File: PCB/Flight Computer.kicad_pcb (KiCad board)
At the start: 6 copper layers, 30 x 60 mm, 75 parts, among them J501 Conn_02x03_Counter_Clockwise, J502 USB_C_Receptacle_USB2.0_16P, J503 Screw_Terminal_01x06, J504 Screw_Terminal_01x04, J505 Conn_01x04, J506 Conn_02x03_Counter_Clockwise, J507 Conn_01x05, J601 Conn_Coaxial, Q701 SL2302S, Q702 SL2302S, Q703 SL2302S, U201 LM1117MP-3.3, U301 W25Q128JVS, U302 STM32F446RETx, U401 MMC5633NJL, U402 LSM6DSV320, U403 MS5607-02BA, U404 SAM-M8Q, U601 RFM95W-915S2, Y301 Resonator

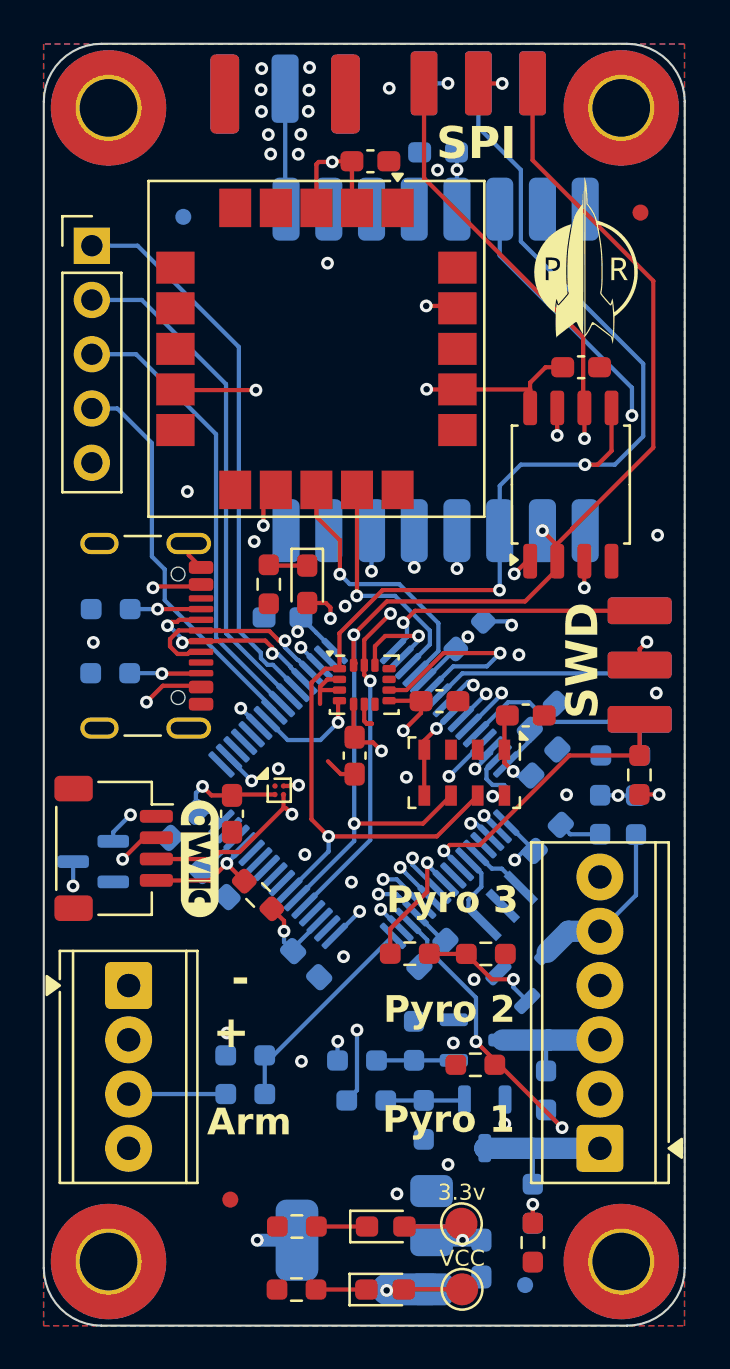
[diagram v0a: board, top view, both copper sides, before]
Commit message: Added buzzer Added 2 more leds to MCU Fixed servo connector GND hole shape Added Servo VCC pin Added additional silkscreen for debug connections Added copper plane text "V1.1" Made 915MHz radio trace 50 Ohm
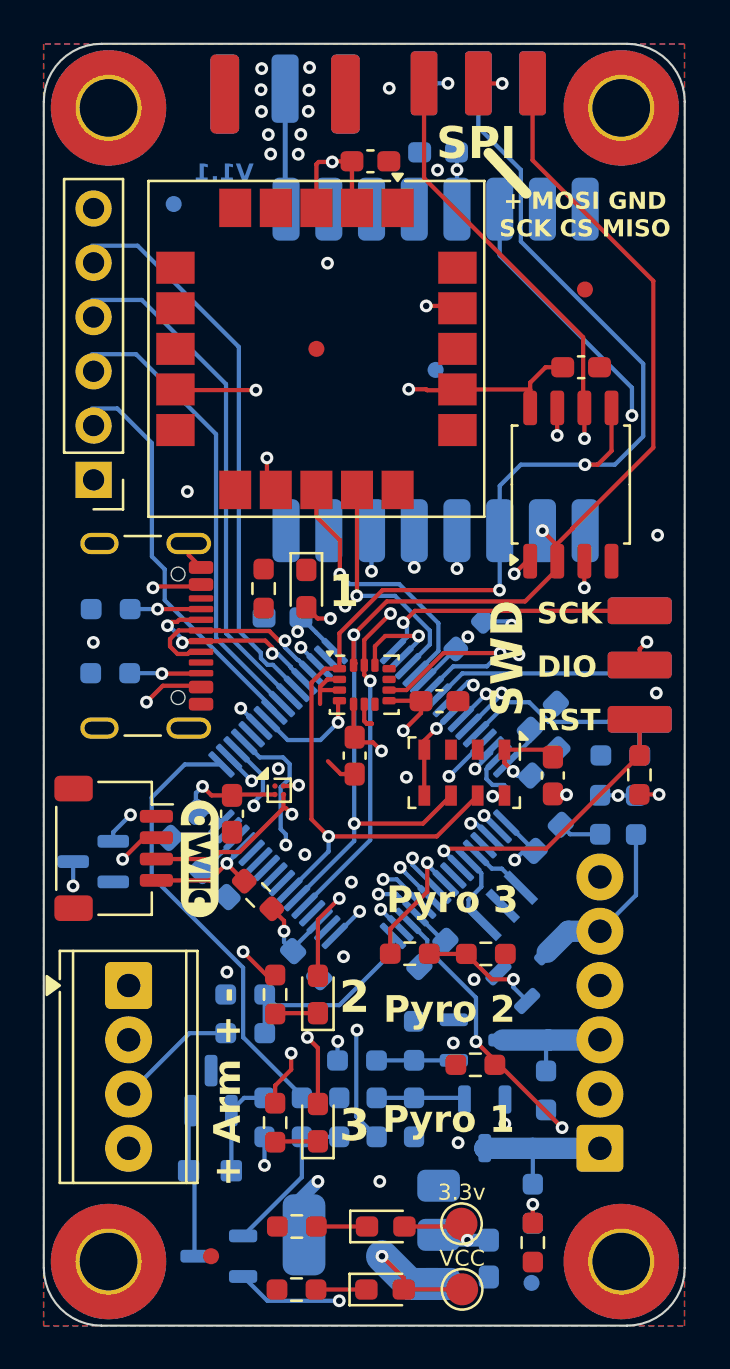
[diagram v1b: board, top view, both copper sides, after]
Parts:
- added BZ501: Buzzer, Buzzer:Buzzer_3mm, B.Cu at (105.4, 105.2)
- added D301: LED, LED_SMD:LED_0603_1608Metric_Pad1.05x0.95mm_HandSolder, F.Cu at (110.0, 78.0)
- added D303: LED, LED_SMD:LED_0603_1608Metric_Pad1.05x0.95mm_HandSolder, F.Cu at (110.5, 103.0)
- added D502: D, Package_TO_SOT_SMD:SOT-23, B.Cu at (105.5, 101.5)
- added FID102: Fiducial, Fiducial:Fiducial_0.75mm_Mask1.5mm, F.Cu at (110.4, 66.8)
- added FID202: Fiducial, Fiducial:Fiducial_0.75mm_Mask1.5mm, B.Cu at (116.0, 67.8)
- added Q1: SL2302S, Package_TO_SOT_SMD:SOT-23-3, B.Cu at (105.9, 109.2)
- added R1: 500, Resistor_SMD:R_0603_1608Metric_Pad0.98x0.95mm_HandSolder, B.Cu at (109.8, 102.8)
- added R2: 10k, Resistor_SMD:R_0603_1608Metric_Pad0.98x0.95mm_HandSolder, B.Cu at (111.5, 102.8)
- added R305: 1k, Resistor_SMD:R_0603_1608Metric_Pad0.98x0.95mm_HandSolder, F.Cu at (108.0, 78.0)
- added R307: 1k, Resistor_SMD:R_0603_1608Metric_Pad0.98x0.95mm_HandSolder, F.Cu at (108.5, 103.0)
- added R503: R_US, Resistor_SMD:R_0603_1608Metric_Pad0.98x0.95mm_HandSolder, B.Cu at (108.0, 102.8)
- G***, J503: moved to B.Cu
- J507: value Conn_01x05 -> Conn_01x06; footprint Connector_PinHeader_2.54mm:PinHeader_1x05_P2.54mm_Vertical -> Connector_PinHeader_2.54mm:PinHeader_1x06_P2.54mm_Vertical
- moved D302 19.2 mm to (110.5, 97.0), turned to 90 degrees
- moved R306 19.2 mm to (108.5, 97.0), turned to -90 degrees
- moved G*** 17.7 mm to (105.2, 63.5), turned to 180 degrees
- moved J507 11.0 mm to (100.0, 72.9), turned to 180 degrees
- moved FID101 4.44 mm to (123.0, 64.0)
- moved C404 3.08 mm to (121.5, 86.8), turned to -90 degrees
- moved R701 2.85 mm to (107.1, 98.8)
- moved R704 2.85 mm to (107.1, 97.0)
- moved FID103 2.80 mm to (105.5, 109.2)
- moved R702 0.93 mm to (113.2, 102.8), turned to 90 degrees
- moved FID201 0.75 mm to (103.8, 60.0)
- moved R705 0.47 mm to (115.0, 102.8)
- moved U201 0.41 mm to (113.0, 108.2)
- moved C201 0.35 mm to (118.5, 109.4)
- moved FID203 0.32 mm to (120.5, 110.5)
- renumbered D301 to D302, FID102 to FID103, FID103 to FID201, FID104 to FID203, R305 to R306
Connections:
- D302 pad 2: /MCU_LED -> /MCU_LED2
- J507 pad 1: /Servo1 -> GND
- J507 pad 2: /Servo2 -> VCC
- J507 pad 3: /Servo3 -> /Servo4
- J507 pad 4: /Servo4 -> /Servo3
- J507 pad 5: GND -> /Servo2
- U302 pad 34: /MCU_LED -> /MCU_LED1
- U302 pad 35: /MCU/PB14 -> /MCU_LED2
- U302 pad 36: /MCU/PB15 -> /MCU_LED3
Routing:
- net VCC: track 43.1 -> 81.9 mm, vias 2 -> 3
- net /Buzzer: track 0.00 -> 20.9 mm
- net /MCU_LED3: track 0.00 -> 19.4 mm, vias 0 -> 2
- net /MCU_LED2: track 0.00 -> 14.2 mm, vias 0 -> 2
- net /MCU_LED: track 13.5 -> 0.00 mm, vias 2 -> 0
- net /MCU_LED1: track 0.00 -> 13.1 mm, vias 0 -> 2
- net GND: track 14.6 -> 24.2 mm, vias 34 -> 35
- net Net-(Q1-G): track 0.00 -> 7.53 mm
- net Net-(BZ501--): track 0.00 -> 7.09 mm
- net Net-(BZ501-+): track 0.00 -> 4.61 mm
- net /I2C_SCL: track 27.3 -> 31.1 mm
- net Net-(D303-K): track 0.00 -> 2.07 mm
- net +3.3V: track 64.5 -> 66.5 mm
- net /Pyro1_Trigger: track 14.0 -> 15.5 mm
- net Pyro_Power: track 44.6 -> 45.8 mm
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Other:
- board text added: "+"
- board text added: "+ Arm + -"
- board text added: "+ MOSI GND SCK CS MISO"
- board text added: "-"
- board text added: "1"
- board text added: "2"
- board text added: "3"
- board text added: "4"
- board text added: "B"
- board text added: "DIO"
- board text added: "GND"
- board text added: "RST"
- board text added: "SCK"
- board text added: "SWO"
- board text added: "Servos"
- board text added: "V1.1"
- board text removed: "+ -"
- board text removed: "Arm"

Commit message: Fixed some mistakes
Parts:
- J503: moved to F.Cu
- moved R701 0.33 mm to (107.0, 98.5)
- moved R704 0.27 mm to (107.0, 96.8)
- moved D502 0.19 mm to (105.5, 101.3)
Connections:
- R503 pad 1: VCC -> +3.3V
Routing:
- net +3.3V: track 66.5 -> 68.2 mm, vias 17 -> 18
- net VCC: track 81.9 -> 80.6 mm, vias 3 -> 2
- net /Servo4: track 18.4 -> 19.4 mm
- net /Servo3: track 21.3 -> 21.9 mm
- net /Servo1: track 26.1 -> 26.8 mm
- net /Servo2: track 23.8 -> 24.4 mm

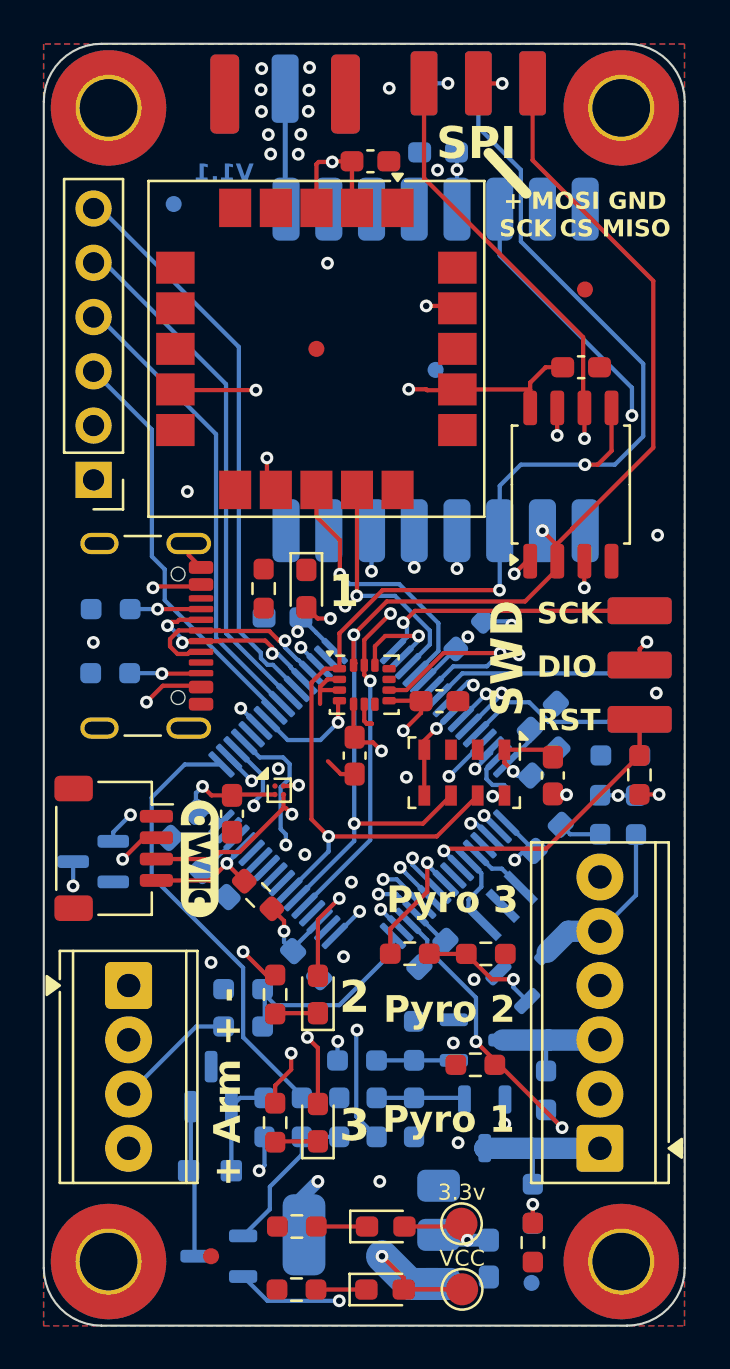
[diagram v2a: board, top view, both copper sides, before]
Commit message: Switched MISO and MOSI for IMU, fixed some DRC Errors
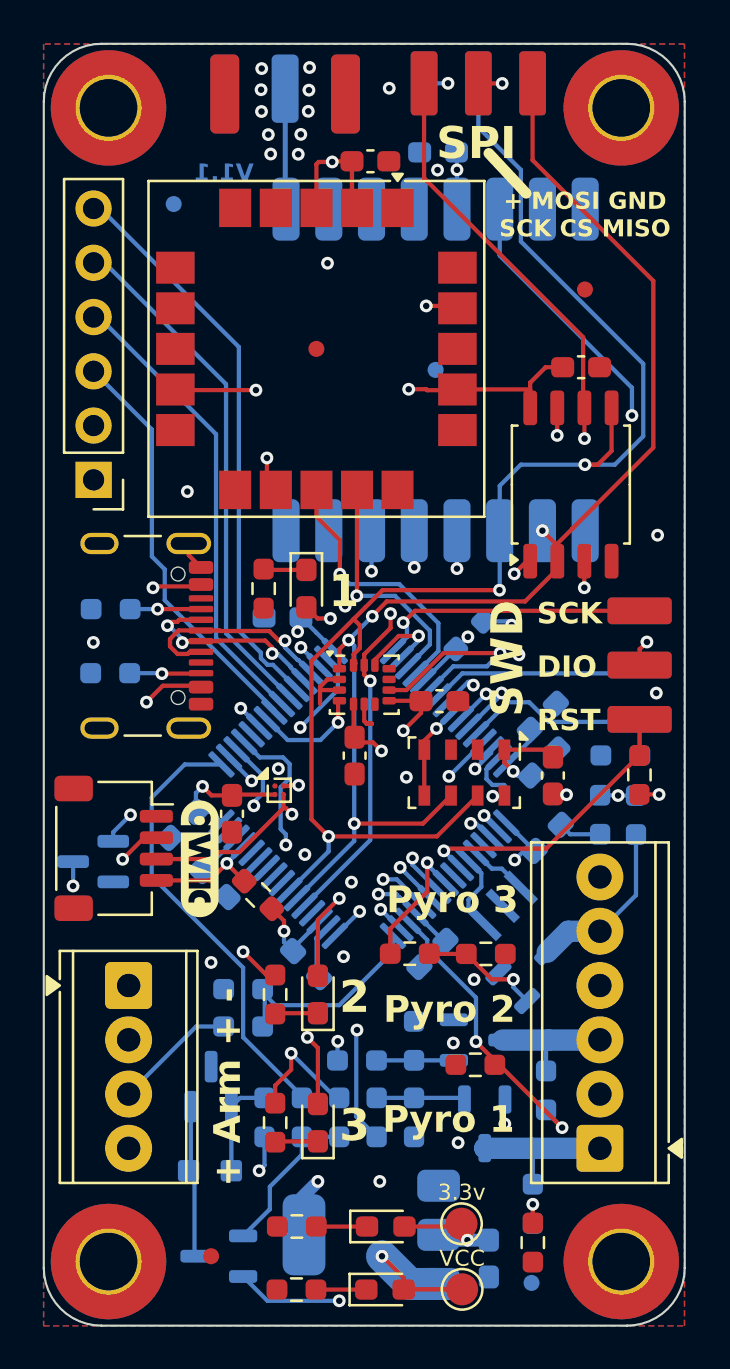
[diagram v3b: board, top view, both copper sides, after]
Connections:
- U402 pad 1: /SPI_MOSI -> /SPI_MISO
- U402 pad 14: /SPI_MISO -> /SPI_MOSI
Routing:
- net GND: track 24.2 -> 31.8 mm, vias 35 -> 36
- net /SPI_MOSI: track 66.1 -> 68.4 mm
- net Net-(D301-K): track 0.05 -> 2.07 mm
- net VCC: track 80.6 -> 79.3 mm
- net /SPI_MISO: vias 3 -> 4
- added copper zone on In1.Cu, net VCC

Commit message: Tweaked silkscreen, update via count for 3.3V reg VCC trace
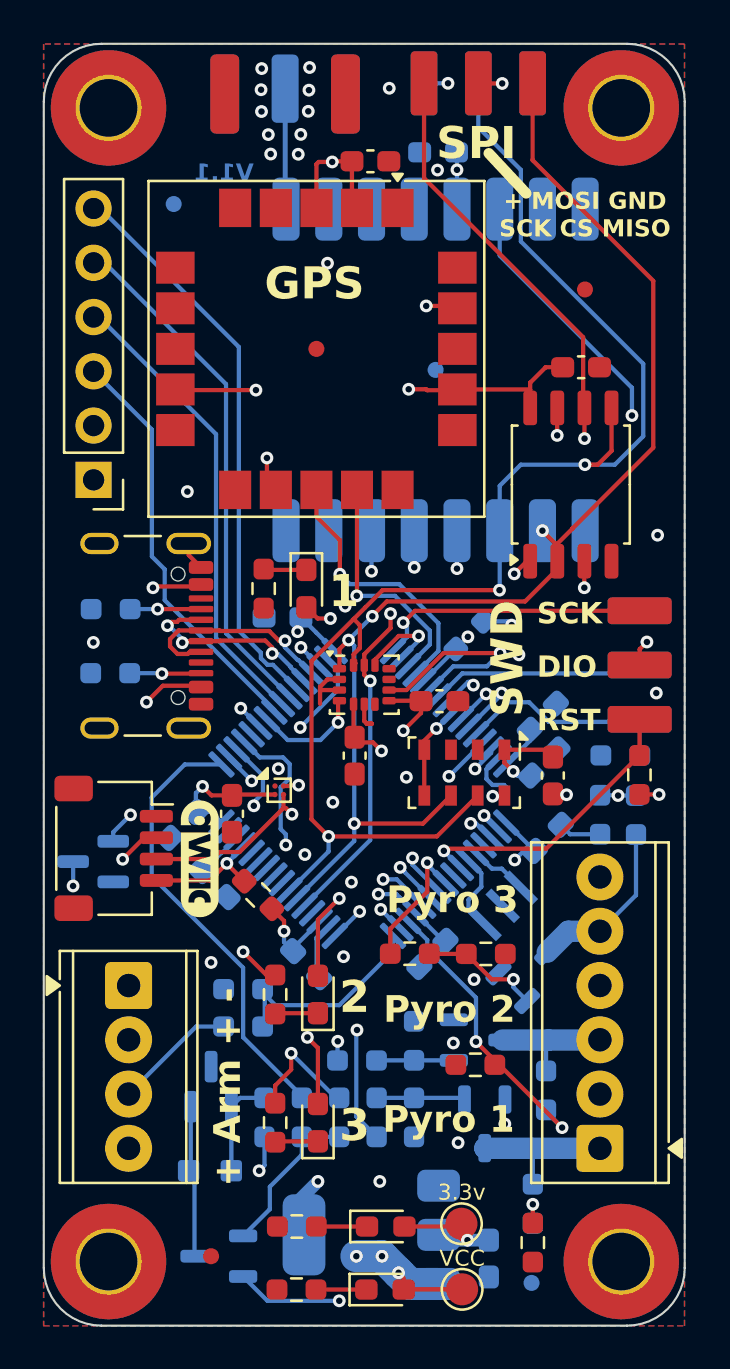
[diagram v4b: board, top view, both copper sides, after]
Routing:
- net VCC: track 79.3 -> 80.1 mm, vias 2 -> 4
- net GND: vias 36 -> 37
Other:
- board text added: "GPS"
- board text added: "Radio"
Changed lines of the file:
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@@
+		)
+	)
+	(gr_text "GPS"
+		(at 108 64.6 0)
+		(layer "F.SilkS" knockout)
+		(effects
+			(font
+				(size 1.5 1.5)
+				(thickness 0.3)
+				(bold yes)
+			)
+			(justify left bottom)
 		)
 	)
@@
 			)
 			(justify left mirror)
+		)
+	)
+	(gr_text "Radio"
+		(at 119.5 65.5 0)
+		(layer "B.SilkS" knockout)
+		(effects
+			(font
+				(size 1.5 1.5)
+				(thickness 0.3)
+				(bold yes)
+			)
+			(justify left bottom mirror)
 		)
 	)
@@
 	)
 	(via
+		(at 111.2 88)
+		(size 0.6)
+		(drill 0.3)
+		(layers "F.Cu" "B.Cu")
+		(free yes)
+		(net 1)
+	)
+	(via
 		(at 110.95 62.77)
 		(size 0.6)
@@
 	)
 	(segment
-		(start 114.5175 110.2675)
-		(end 113.5 109.25)
-		(width 0.2)
-		(layer "F.Cu")
-		(net 6)
-	)
-	(segment
 		(start 117.25 110.8)
 		(end 114.5275 110.8)
@@
 		(net 6)
 	)
+	(via
+		(at 114.275 110.025)
+		(size 0.6)
+		(drill 0.3)
+		(layers "F.Cu" "B.Cu")
+		(net 6)
+	)
+	(via
+		(at 112.3 109.25)
+		(size 0.6)
+		(drill 0.3)
+		(layers "F.Cu" "B.Cu")
+		(net 6)
+	)
+	(segment
+		(start 114.275 110.025)
+		(end 114.8 110.55)
+		(width 1.5)
+		(layer "B.Cu")
+		(net 6)
+	)
+	(segment
+		(start 114.275 110.025)
+		(end 113.5 109.25)
+		(width 1.5)
+		(layer "B.Cu")
+		(net 6)
+	)
 	(segment
 		(start 99.044999 90.78)
@@
 	(segment
 		(start 113.5 109.25)
-		(end 114.8 110.55)
+		(end 112.3 109.25)
 		(width 1.5)
 		(layer "B.Cu")
@@
 	)
 	(segment
+		(start 113.5 109.25)
+		(end 114.275 110.025)
+		(width 1.5)
+		(layer "In3.Cu")
+		(net 6)
+	)
+	(segment
 		(start 99.4 92.28)
 		(end 99.04 91.92)
@@
 	(segment
 		(start 109.3 109.25)
-		(end 106.4 106.35)
+		(end 104.25 104.2)
 		(width 1.5)
 		(layer "In3.Cu")
@@
 	)
 	(segment
+		(start 112.3 109.25)
+		(end 109.3 109.25)
+		(width 1.5)
+		(layer "In3.Cu")
+		(net 6)
+	)
+	(segment
+		(start 99.4 103.77)
+		(end 99.83 104.2)
+		(width 1.5)
+		(layer "In3.Cu")
+		(net 6)
+	)
+	(segment
+		(start 112.3 109.25)
+		(end 113.5 109.25)
+		(width 1.5)
+		(layer "In3.Cu")
+		(net 6)
+	)
+	(segment
 		(start 104.25 104.2)
 		(end 101.64 104.2)
 		(width 1.5)
 		(layer "In3.Cu")
-		(net 6)
-	)
-	(segment
-		(start 106.4 106.35)
-		(end 104.25 104.2)
-		(width 1.5)
-		(layer "In3.Cu")
-		(net 6)
-	)
-	(segment
-		(start 113.5 109.25)
-		(end 109.3 109.25)
-		(width 1.5)
-		(layer "In3.Cu")
-		(net 6)
-	)
-	(segment
-		(start 99.4 103.77)
-		(end 99.83 104.2)
-		(width 1.5)
-		(layer "In3.Cu")

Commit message: Moved compass away from power traces, minor routing changes
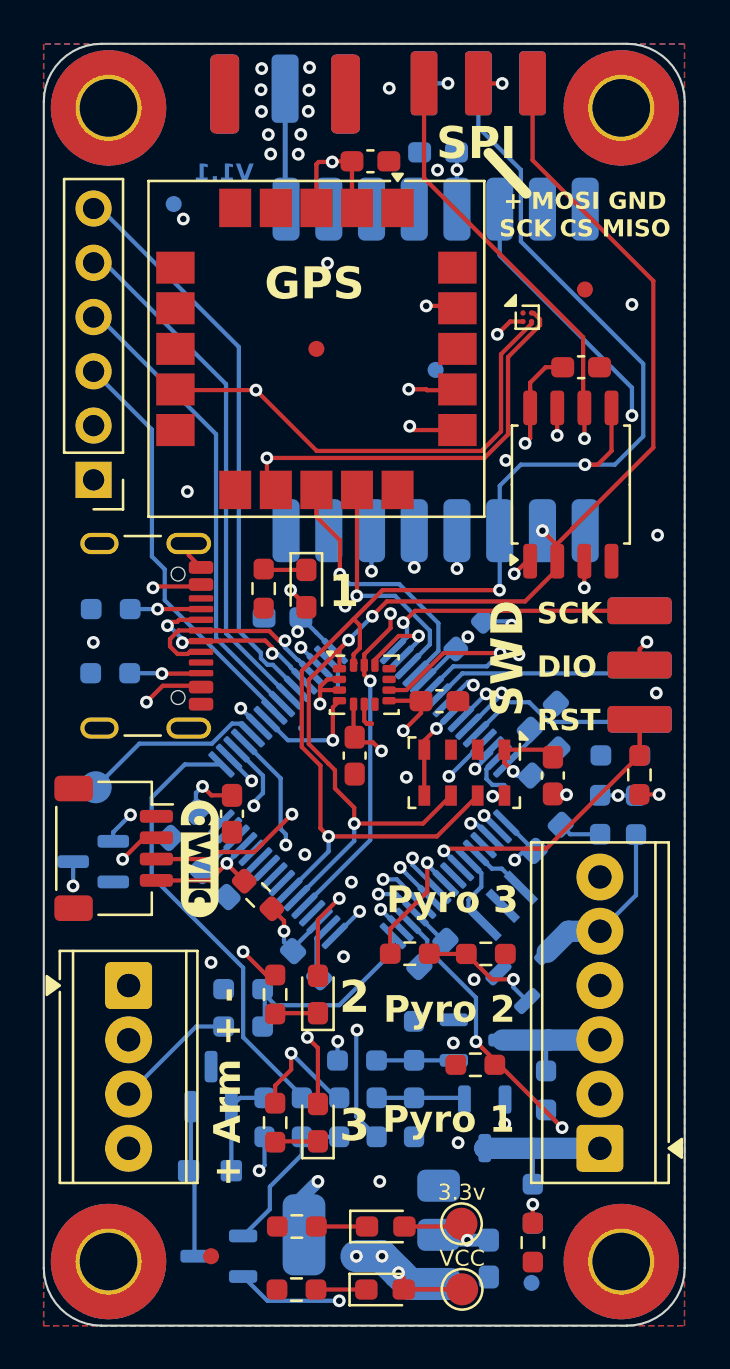
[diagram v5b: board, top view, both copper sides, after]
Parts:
- added TP1: TestPoint, TestPoint:TestPoint_Pad_D1.5mm, B.Cu at (100.1, 87.3)
- moved U401 25.0 mm to (120.3, 65.3)
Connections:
- U302 pad 37: /MCU/PC6 -> /PC6
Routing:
- net /I2C_SDA: track 42.2 -> 60.1 mm
- net /I2C_SCL: track 31.0 -> 48.5 mm, vias 3 -> 2
- net /PC6: track 0.00 -> 8.74 mm
- net +3.3V: track 68.2 -> 66.1 mm, vias 18 -> 20
- net /SPI_MISO: track 59.7 -> 61.3 mm
- net /MCU_LED3: track 19.4 -> 18.4 mm
- net GND: track 31.8 -> 31.7 mm, vias 37 -> 39
